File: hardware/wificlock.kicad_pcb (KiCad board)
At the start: 4 copper layers, 71.8 x 30.5 mm, 41 parts, among them J1 USB_C_Receptacle_USB2.0, Q1 AO3402, Q2 AO3402, Q3 AO3402, Q4 AO3402, SW1 SW_SPST, SW2 SW_SPST, SW3 SW_SPST, U1 CH340C/G, U2 ESP-12F, U3 ME6211C33M5G, U4 HT16K33-20SOP, U5 KW4-56NCLB-P, Y1 12MHz

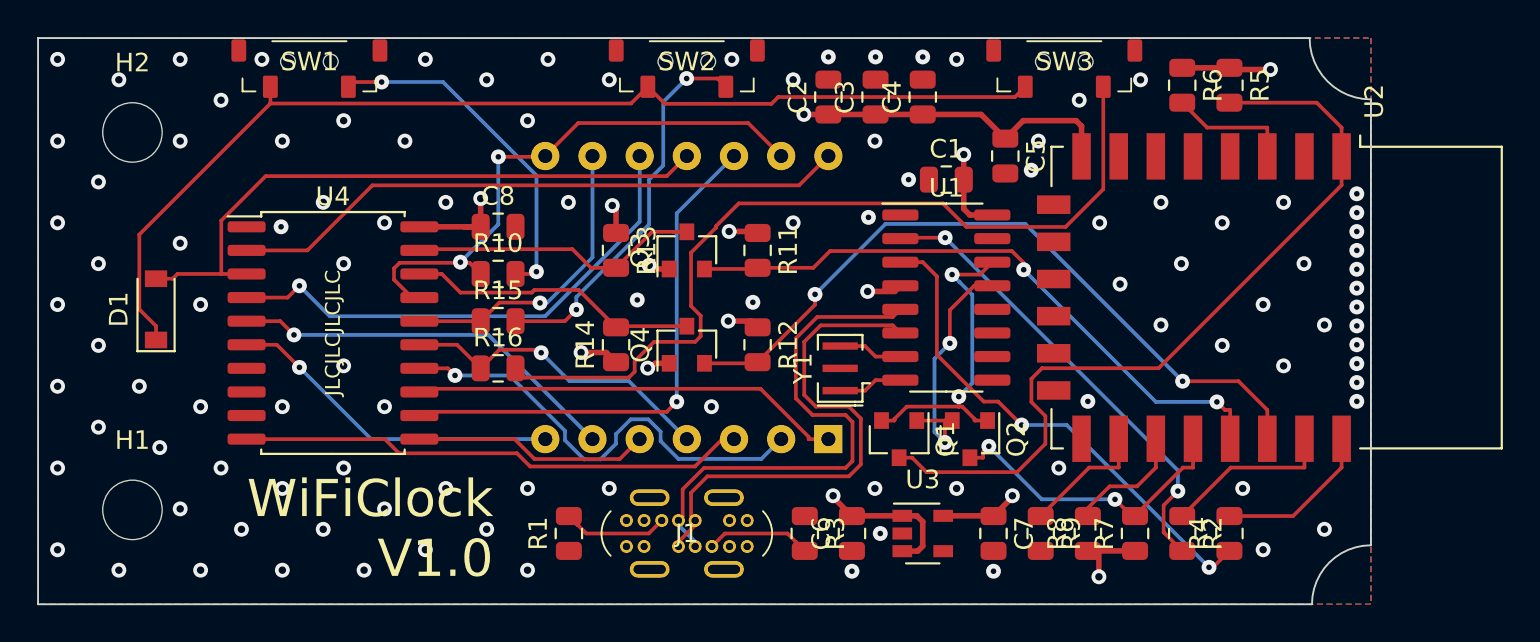
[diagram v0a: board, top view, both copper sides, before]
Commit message: some more minor routing fixes
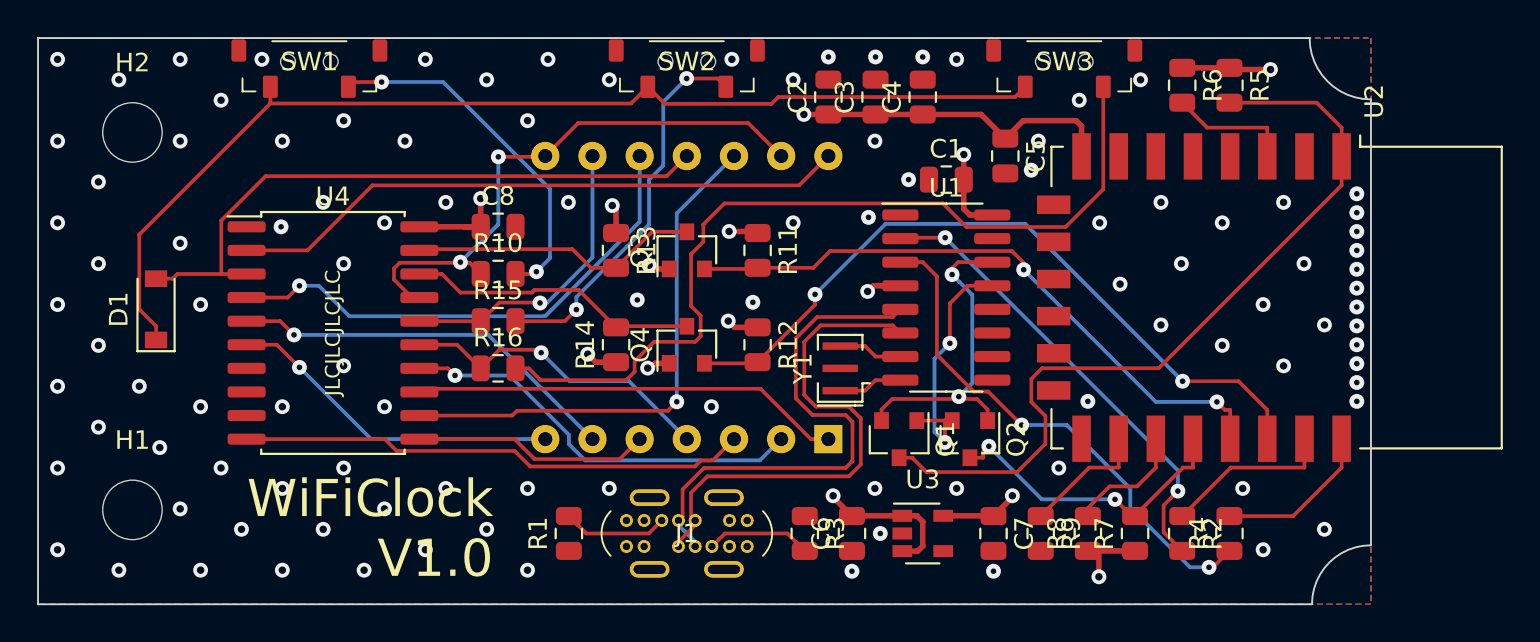
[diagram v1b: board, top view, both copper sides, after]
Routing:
- net ROW3: track 24.6 -> 22.3 mm
- net ~RTS: track 16.7 -> 17.4 mm
- net Net-(R10-Pad2): track 18.7 -> 19.3 mm
- net Net-(R4-Pad1): track 27.4 -> 28.0 mm
- net Net-(R16-Pad2): track 46.4 -> 46.9 mm

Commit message: change via and pad hole sizes to 0.45 mm to match JLCPCB production
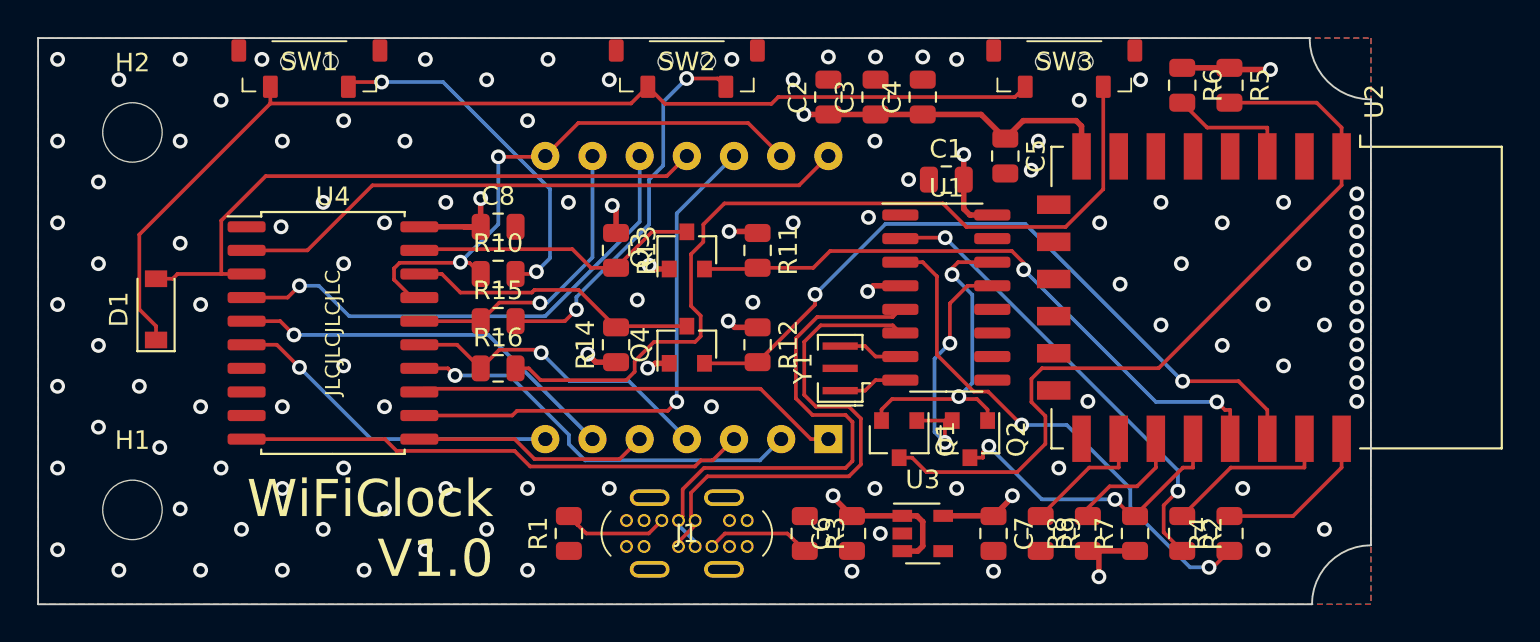
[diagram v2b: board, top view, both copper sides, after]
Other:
- net class Default: via_drill 0.3 -> 0.45
- net class Power: via_drill 0.4 -> 0.45
- net class Shield: via_drill 0.3 -> 0.45

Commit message: add 3D models for footprints
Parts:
- SW1, SW2, SW3: footprint wificlock:Switch-Tactile-3x6x3.5 -> wificlock:SW_SPST_SMD_3x6x3.5_Side

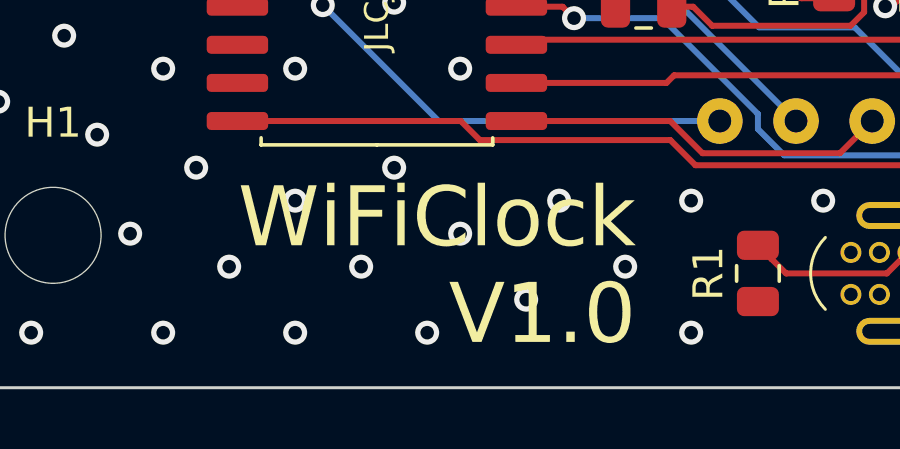
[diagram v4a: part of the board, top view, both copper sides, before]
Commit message: fix display footprint to match actual hardware (only changes silkscreen on PCB)
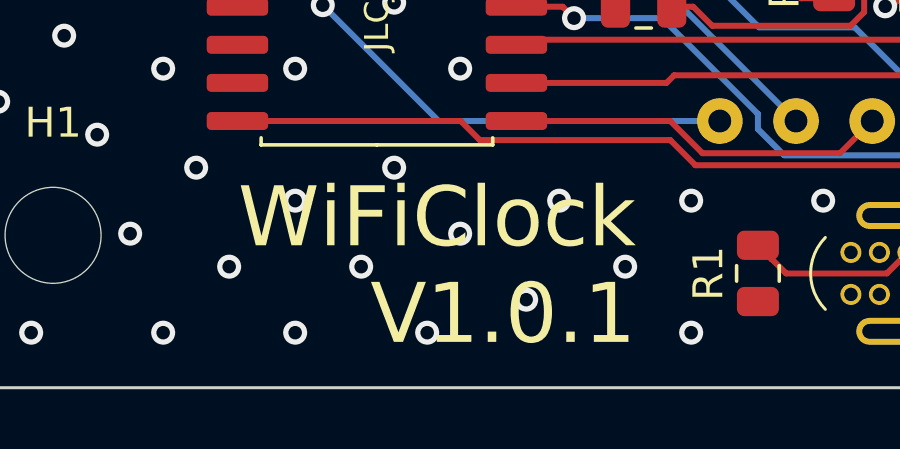
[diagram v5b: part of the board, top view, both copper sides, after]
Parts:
- U5: footprint wificlock:KW4-56NXLB-P -> wificlock:CL5643AH
- moved U5 1.27 mm to (128.3, 127.0)
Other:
- board text added: "WiFiClock V1.0.1"
- board text removed: "WiFiClock V1.0"
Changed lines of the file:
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@@
     (uvia_drill 0.1)
+  )
+  (module wificlock:CL5643AH (layer B.Cu)
+    (at 128.27 127 180)
+    (descr "4-digit 7-segment display with four dots and colon")
+    (fp_text reference U5 (at 0 -0.8) (layer B.SilkS)
+      (effects (font (size 1 1) (thickness 0.15)) (justify mirror))
+    )
+    (fp_text value KW4-56NCLB-P (at 0 0.2) (layer B.Fab)
+      (effects (font (size 1 1) (thickness 0.15)) (justify mirror))
+    )
+    (fp_line (start 25.55 9.9) (end -25.55 9.9) (layer B.CrtYd) (width 0.05))
+    (fp_line (start 25.55 -9.9) (end 25.55 9.9) (layer B.CrtYd) (width 0.05))
+    (fp_line (start -25.55 -9.9) (end 25.55 -9.9) (layer B.CrtYd) (width 0.05))
+    (fp_line (start -25.55 9.9) (end -25.55 -9.9) (layer B.CrtYd) (width 0.05))
+    (fp_line (start 25.35 9.7) (end -25.35 9.7) (layer B.SilkS) (width 0.12))
+    (fp_line (start 25.35 -9.7) (end 25.35 9.7) (layer B.SilkS) (width 0.12))
+    (fp_line (start -25.35 -9.7) (end 25.35 -9.7) (layer B.SilkS) (width 0.12))
+    (fp_line (start -25.35 9.7) (end -25.35 -9.7) (layer B.SilkS) (width 0.12))
+    (fp_line (start -25.15 9.5) (end 25.15 9.5) (layer B.Fab) (width 0.1))
+    (fp_line (start 25.15 9.5) (end 25.15 -9.5) (layer B.Fab) (width 0.1))
+    (fp_line (start 25.15 -9.5) (end -25.15 -9.5) (layer B.Fab) (width 0.1))
+    (fp_line (start -25.15 -9.5) (end -25.15 9.5) (layer B.Fab) (width 0.1))
+    (pad 14 thru_hole circle (at -6.35 7.62 180) (size 1.524 1.524) (drill 0.762) (layers *.Cu *.Mask)
+      (net 41 COM0))
+    (pad 13 thru_hole circle (at -3.81 7.62 180) (size 1.524 1.524) (drill 0.762) (layers *.Cu *.Mask)
+      (net 26 K1))
+    (pad 12 thru_hole circle (at -1.27 7.62 180) (size 1.524 1.524) (drill 0.762) (layers *.Cu *.Mask)
+      (net 35 ROW5))
+    (pad 11 thru_hole circle (at 1.27 7.62 180) (size 1.524 1.524) (drill 0.762) (layers *.Cu *.Mask)
+      (net 4 COM1))
+    (pad 10 thru_hole circle (at 3.81 7.62 180) (size 1.524 1.524) (drill 0.762) (layers *.Cu *.Mask)
+      (net 40 COM2))
+    (pad 9 thru_hole circle (at 6.35 7.62 180) (size 1.524 1.524) (drill 0.762) (layers *.Cu *.Mask)
+      (net 28 K2))
+    (pad 8 thru_hole circle (at 8.89 7.62 180) (size 1.524 1.524) (drill 0.762) (layers *.Cu *.Mask)
+      (net 26 K1))
+    (pad 7 thru_hole circle (at 8.89 -7.62 180) (size 1.524 1.524) (drill 0.762) (layers *.Cu *.Mask)
+      (net 38 COM4))
+    (pad 6 thru_hole circle (at 6.35 -7.62 180) (size 1.524 1.524) (drill 0.762) (layers *.Cu *.Mask)
+      (net 39 COM3))
+    (pad 5 thru_hole circle (at 3.81 -7.62 180) (size 1.524 1.524) (drill 0.762) (layers *.Cu *.Mask)
+      (net 36 ROW6))
+    (pad 4 thru_hole circle (at 1.27 -7.62 180) (size 1.524 1.524) (drill 0.762) (layers *.Cu *.Mask)
+      (net 30 K3))
+    (pad 3 thru_hole circle (at -1.27 -7.62 180) (size 1.524 1.524) (drill 0.762) (layers *.Cu *.Mask)
+      (net 37 ROW7))
+    (pad 2 thru_hole circle (at -3.81 -7.62 180) (size 1.524 1.524) (drill 0.762) (layers *.Cu *.Mask)
+      (net 33 ROW3))
+    (pad 1 thru_hole rect (at -6.35 -7.62 180) (size 1.524 1.524) (drill 0.762) (layers *.Cu *.Mask)
+      (net 34 ROW4))
+    (model ${KIPRJMOD}/wificlock.pretty/CL5643AH.step
+      (at (xyz 0 0 0))
+      (scale (xyz 1 1 1))
+      (rotate (xyz 0 0 0))
+    )
   )
   (module wificlock:USB_C_Receptacle_UT03FD014SX01ZA_Vertical (layer F.Cu)
@@
       (effects (font (size 1 1) (thickness 0.15)))
     )
-    (fp_arc (start 2.89 0) (end 4.1 1.2) (angle -89.52451908) (layer F.SilkS) (width 0.1))
-    (fp_arc (start -2.89 0) (end -4.1 -1.2) (angle -89.52451908) (layer F.SilkS) (width 0.1))
-    (fp_arc (start 2.89 0) (end 2.89 -1.58) (angle 180) (layer F.Fab) (width 0.12))
-    (fp_arc (start -2.89 0) (end -2.89 -1.58) (angle -180) (layer F.Fab) (width 0.12))
     (fp_line (start -4.9 2.8) (end -4.9 -2.8) (layer F.CrtYd) (width 0.05))
     (fp_line (start 4.9 2.8) (end -4.9 2.8) (layer F.CrtYd) (width 0.05))
@@
     (fp_line (start -2.89 -1.58) (end 2.89 -1.58) (layer F.Fab) (width 0.12))
     (fp_line (start -2.89 1.58) (end 2.89 1.58) (layer F.Fab) (width 0.12))
+    (fp_arc (start 2.89 0) (end 4.1 1.2) (angle -89.52451908) (layer F.SilkS) (width 0.1))
+    (fp_arc (start -2.89 0) (end -4.1 -1.2) (angle -89.52451908) (layer F.SilkS) (width 0.1))
+    (fp_arc (start 2.89 0) (end 2.89 -1.58) (angle 180) (layer F.Fab) (width 0.12))
+    (fp_arc (start -2.89 0) (end -2.89 -1.58) (angle -180) (layer F.Fab) (width 0.12))
     (pad B8 smd circle (at 4.1 1.7) (size 0.4 0.4) (layers Dwgs.User))
     (pad A8 smd circle (at 4.1 -1.7) (size 0.4 0.4) (layers Dwgs.User))
@@
     (pad "" np_thru_hole circle (at -1.15 0) (size 0.8 0.8) (drill 0.8) (layers *.Cu *.Mask))
     (model ${KIPRJMOD}/wificlock.pretty/SW_SPST_SMD_3x6x3.5_Side.step
-      (at (xyz 0 0 0))
-      (scale (xyz 1 1 1))
-      (rotate (xyz 0 0 0))
-    )
-  )
-  (module wificlock:KW4-56NXLB-P (layer B.Cu)
-    (at 127 127 180)
-    (fp_text reference U5 (at 0 -0.8) (layer B.SilkS)
-      (effects (font (size 1 1) (thickness 0.15)) (justify mirror))
-    )
-    (fp_text value KW4-56NCLB-P (at 0 0.2) (layer B.Fab)
-      (effects (font (size 1 1) (thickness 0.15)) (justify mirror))
-    )
-    (fp_line (start 25.55 9.9) (end -25.55 9.9) (layer B.CrtYd) (width 0.05))
-    (fp_line (start 25.55 -9.9) (end 25.55 9.9) (layer B.CrtYd) (width 0.05))
-    (fp_line (start -25.55 -9.9) (end 25.55 -9.9) (layer B.CrtYd) (width 0.05))
-    (fp_line (start -25.55 9.9) (end -25.55 -9.9) (layer B.CrtYd) (width 0.05))
-    (fp_line (start 25.35 9.7) (end -25.35 9.7) (layer B.SilkS) (width 0.12))
-    (fp_line (start 25.35 -9.7) (end 25.35 9.7) (layer B.SilkS) (width 0.12))
-    (fp_line (start -25.35 -9.7) (end 25.35 -9.7) (layer B.SilkS) (width 0.12))
-    (fp_line (start -25.35 9.7) (end -25.35 -9.7) (layer B.SilkS) (width 0.12))
-    (fp_line (start -25.15 9.5) (end 25.15 9.5) (layer B.Fab) (width 0.1))
-    (fp_line (start 25.15 9.5) (end 25.15 -9.5) (layer B.Fab) (width 0.1))
-    (fp_line (start 25.15 -9.5) (end -25.15 -9.5) (layer B.Fab) (width 0.1))
-    (fp_line (start -25.15 -9.5) (end -25.15 9.5) (layer B.Fab) (width 0.1))
-    (pad 14 thru_hole circle (at -7.62 7.62 180) (size 1.524 1.524) (drill 0.762) (layers *.Cu *.Mask)
-      (net 41 COM0))
-    (pad 13 thru_hole circle (at -5.08 7.62 180) (size 1.524 1.524) (drill 0.762) (layers *.Cu *.Mask)
-      (net 26 K1))
-    (pad 12 thru_hole circle (at -2.54 7.62 180) (size 1.524 1.524) (drill 0.762) (layers *.Cu *.Mask)
-      (net 35 ROW5))
-    (pad 11 thru_hole circle (at 0 7.62 180) (size 1.524 1.524) (drill 0.762) (layers *.Cu *.Mask)
-      (net 4 COM1))
-    (pad 10 thru_hole circle (at 2.54 7.62 180) (size 1.524 1.524) (drill 0.762) (layers *.Cu *.Mask)
-      (net 40 COM2))
-    (pad 9 thru_hole circle (at 5.08 7.62 180) (size 1.524 1.524) (drill 0.762) (layers *.Cu *.Mask)
-      (net 28 K2))
-    (pad 8 thru_hole circle (at 7.62 7.62 180) (size 1.524 1.524) (drill 0.762) (layers *.Cu *.Mask)
-      (net 26 K1))
-    (pad 7 thru_hole circle (at 7.62 -7.62 180) (size 1.524 1.524) (drill 0.762) (layers *.Cu *.Mask)
-      (net 38 COM4))
-    (pad 6 thru_hole circle (at 5.08 -7.62 180) (size 1.524 1.524) (drill 0.762) (layers *.Cu *.Mask)
-      (net 39 COM3))
-    (pad 5 thru_hole circle (at 2.54 -7.62 180) (size 1.524 1.524) (drill 0.762) (layers *.Cu *.Mask)
-      (net 36 ROW6))
-    (pad 4 thru_hole circle (at 0 -7.62 180) (size 1.524 1.524) (drill 0.762) (layers *.Cu *.Mask)
-      (net 30 K3))
-    (pad 3 thru_hole circle (at -2.54 -7.62 180) (size 1.524 1.524) (drill 0.762) (layers *.Cu *.Mask)
-      (net 37 ROW7))
-    (pad 2 thru_hole circle (at -5.08 -7.62 180) (size 1.524 1.524) (drill 0.762) (layers *.Cu *.Mask)
-      (net 33 ROW3))
-    (pad 1 thru_hole rect (at -7.62 -7.62 180) (size 1.524 1.524) (drill 0.762) (layers *.Cu *.Mask)
-      (net 34 ROW4))
-    (model ${KIPRJMOD}/wificlock.pretty/KW4-56NXLB-P.step
       (at (xyz 0 0 0))
       (scale (xyz 1 1 1))
@@
     (effects (font (size 0.8 0.8) (thickness 0.15)))
   )
-  (gr_text "WiFiClock\nV1.0" (at 116.586 139.446) (layer F.SilkS)
+  (gr_text "WiFiClock\nV1.0.1" (at 116.586 139.446) (layer F.SilkS)
     (effects (font (size 2 2) (thickness 0.3)) (justify right))
   )

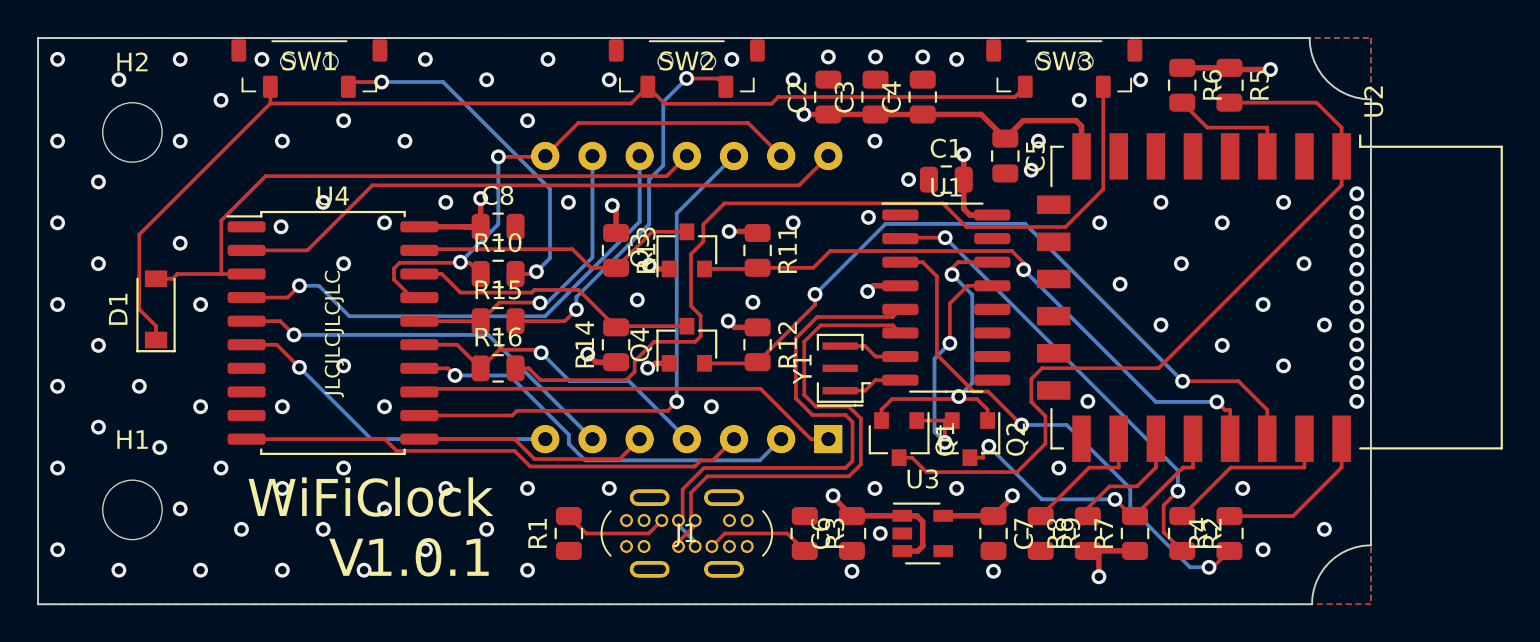
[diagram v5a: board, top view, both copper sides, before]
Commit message: move components to align (center) display, USB receptacle and switches; minor routing optimizations; update Gerber files
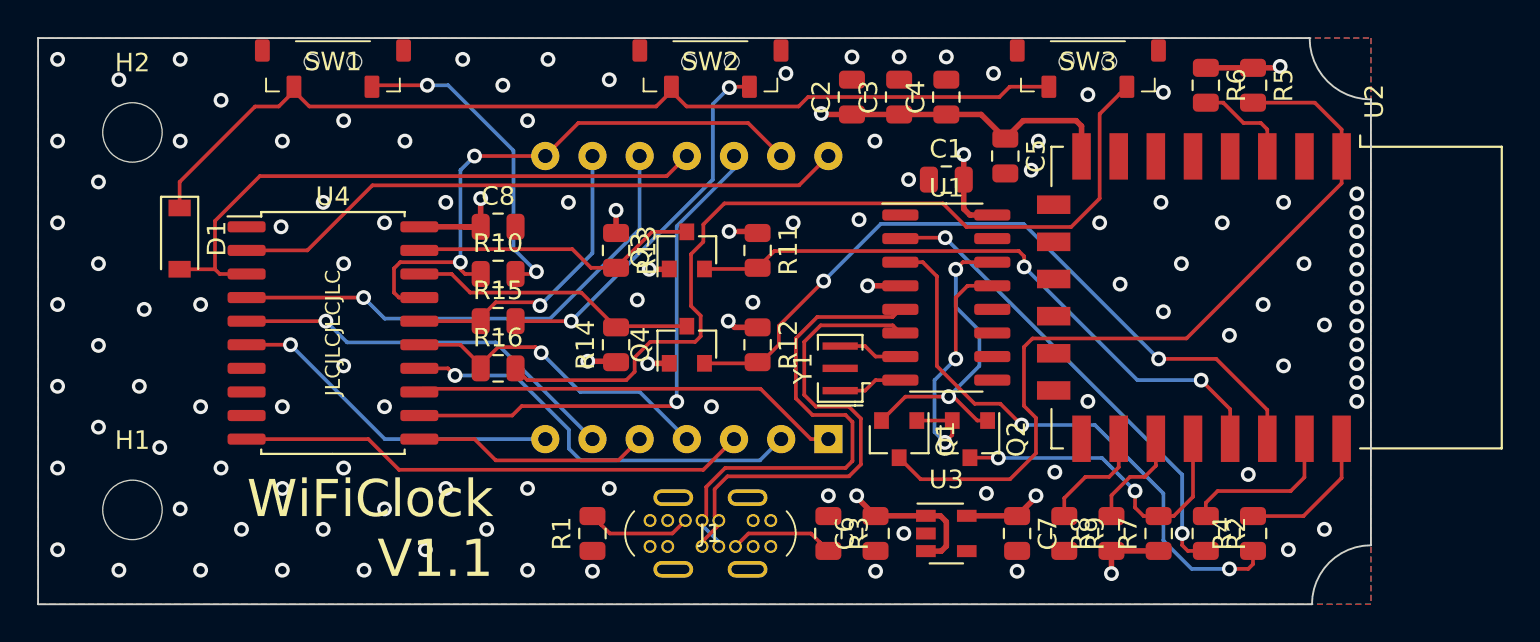
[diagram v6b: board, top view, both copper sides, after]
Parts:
- moved D1 4.02 mm to (99.7, 123.8), turned to 270 degrees
- moved C3 1.27 mm to (138.4, 116.2)
- moved C4 1.27 mm to (141.0, 116.2)
- moved C6 1.27 mm to (137.2, 139.7)
- moved C7 1.27 mm to (144.8, 139.7)
- moved J1 1.27 mm to (128.3, 139.7)
- moved R2 1.27 mm to (154.9, 139.7)
- moved R3 1.27 mm to (134.6, 139.7)
- moved R6 1.27 mm to (154.9, 115.6)
- moved R7 1.27 mm to (152.4, 139.7)
- moved R8 1.27 mm to (149.9, 139.7)
- moved SW2 1.27 mm to (128.3, 114.3)
- moved SW3 1.27 mm to (148.6, 114.3)
- moved U3 1.27 mm to (141.0, 139.7)
- moved R1 1.27 mm to (121.9, 139.7)
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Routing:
- net Net-(D1-Pad1): track 58.7 -> 52.6 mm
- net Net-(R4-Pad1): track 28.0 -> 31.0 mm
- net +3V3: track 42.9 -> 40.8 mm
- net Net-(R10-Pad2): track 19.3 -> 17.3 mm
- net K1: track 30.7 -> 32.1 mm
- net EN: track 6.69 -> 5.36 mm
- net COM1: track 34.4 -> 33.2 mm
- net D+: track 28.5 -> 27.3 mm
- net D-: track 27.8 -> 26.6 mm
- net TXD: track 8.67 -> 7.73 mm
- net GPIO2: track 6.54 -> 5.62 mm
- net Net-(R16-Pad2): track 46.9 -> 47.8 mm
- net GPIO0: track 16.6 -> 17.4 mm
- net RXD: track 9.21 -> 8.67 mm
- net Net-(R15-Pad2): track 20.7 -> 20.2 mm
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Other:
- board text added: "WiFiClock V1.1"
- board text removed: "WiFiClock V1.0.1"
